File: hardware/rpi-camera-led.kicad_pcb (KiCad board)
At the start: 2 copper layers, 25 x 23.9 mm, 24 parts, among them J1 FFC 15P 1.0mm bottom contact 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, J2 FFC 15P 1.0mm top contact (to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, J3 Qwiic (JST SH 1.0mm), J4 SWD program header 2.54mm, Q1 AO3400A, Q2 Phototransistor, U1 CH32V003A4M6

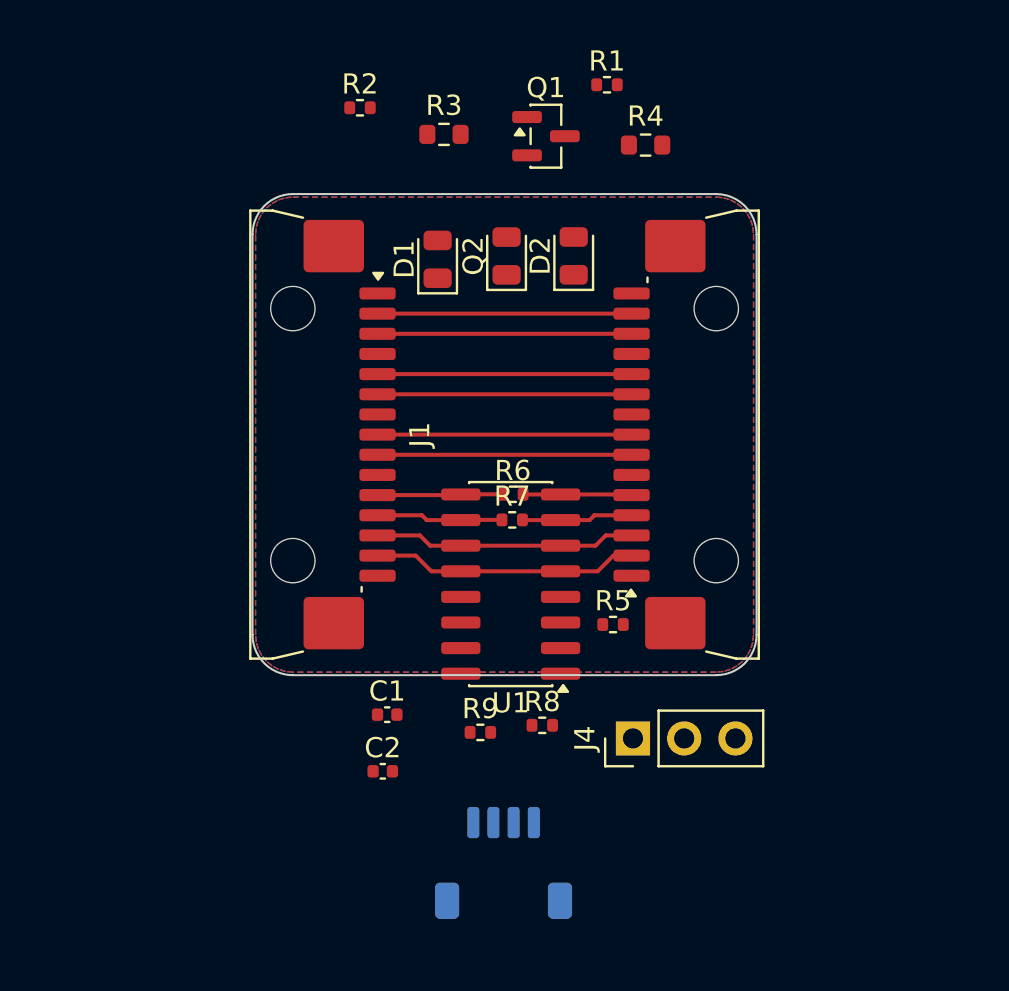
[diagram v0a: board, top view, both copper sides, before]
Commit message: Route camera interposer and prepare manufacturing outputs
Update the CH32V003A4M6 pin mapping, widen and route the board around the camera lens, source the BOM, and add a DRC-gated fabrication export plus approximate assembly CAD renders.

Co-authored-by: Copilot <223556219+Copilot@users.noreply.github.com>
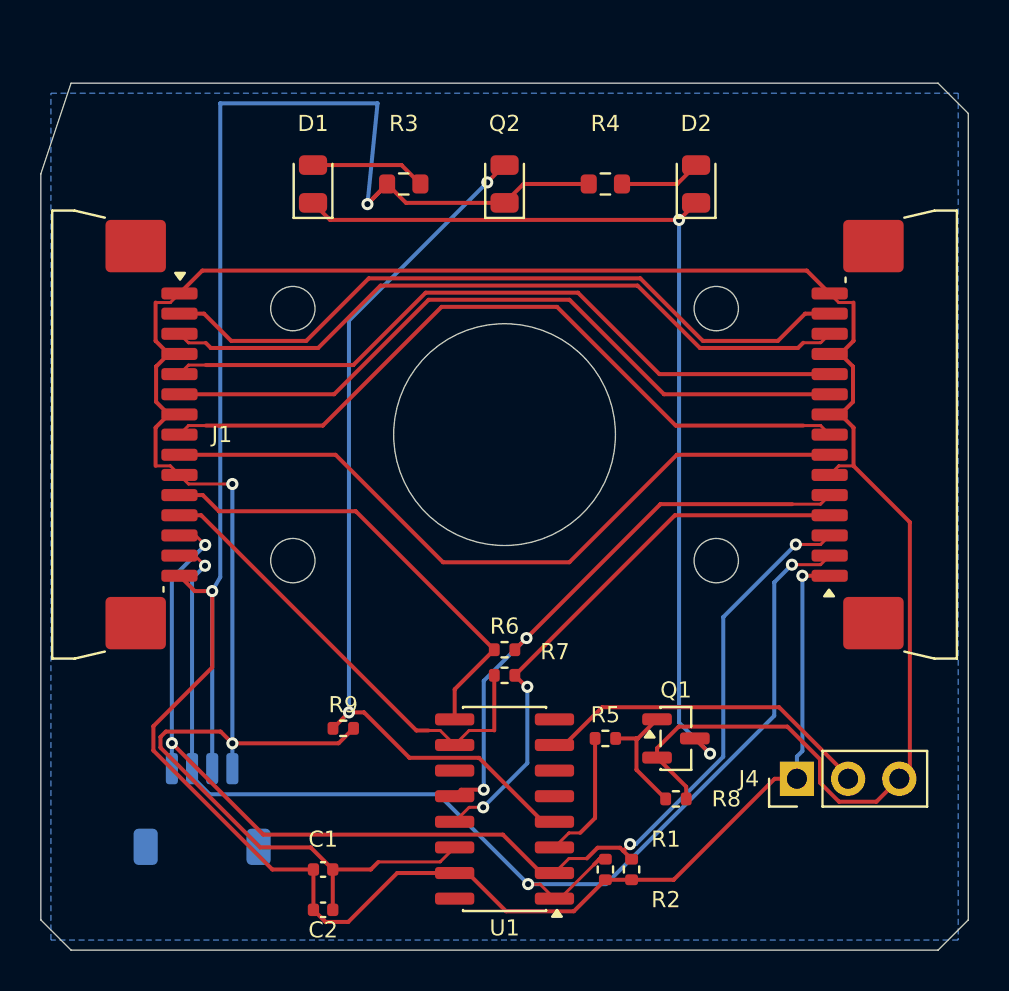
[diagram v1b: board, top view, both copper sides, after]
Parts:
- R3, R4: value 10R -> 47R
- R6, R7: value 0 -> 10k
- moved R2 40.1 mm to (38.8, 53.5), turned to 90 degrees
- moved R1 38.9 mm to (37.5, 53.5), turned to 90 degrees
- moved Q1 30.6 mm to (41.0, 47.0)
- moved J3 15.2 mm to (17.5, 50.5)
- moved U1 11.2 mm to (32.5, 50.5)
- moved J2 9.83 mm to (52.0, 31.9)
- moved J1 9.82 mm to (13.0, 31.9)
- moved J4 8.37 mm to (47.0, 49.0)
- moved C1 8.31 mm to (23.5, 53.5)
- moved R6 7.72 mm to (32.5, 42.6)
- moved R7 7.72 mm to (32.5, 43.9)
- moved R8 7.57 mm to (41.0, 50.0)
- moved C2 7.48 mm to (23.5, 55.5)
- moved D1 7.22 mm to (23.0, 19.5)
- moved D2 7.04 mm to (42.0, 19.5)
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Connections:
- J4 pad 2: CAM_IO1 -> SWIO
- U1 pad 11: SCL -> unconnected-(U1-PD7-Pad11)
- U1 pad 12: SDA -> CAM_IO0
- U1 pad 13: unconnected-(U1-PA2-Pad13) -> CAM_IO1
- U1 pad 5: SDA -> unconnected-(U1-PC6-Pad5)
- U1 pad 6: SCL -> unconnected-(U1-PC7-Pad6)
- U1 pad 7: CAM_IO1 -> SWIO
- U1 pad 8: CAM_IO0 -> unconnected-(U1-PD4-Pad8)
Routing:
- net GND: track 0.00 -> 141.5 mm, vias 0 -> 2
- net 3V3: track 0.00 -> 123.2 mm, vias 0 -> 3
- net SDA: track 13.2 -> 61.6 mm, vias 0 -> 3
- net LED_SW: track 0.00 -> 47.9 mm, vias 0 -> 2
- net SCL: track 13.0 -> 60.3 mm, vias 0 -> 4
- net LIGHT_SENSE: track 0.00 -> 43.9 mm, vias 0 -> 2
- net CAM_CK_N: track 12.6 -> 37.5 mm
- net CAM_CK_P: track 12.6 -> 36.7 mm
- net CAM_D1_P: track 12.6 -> 36.1 mm
- net CAM_IO0: track 5.40 -> 28.8 mm, vias 0 -> 2
- net CAM_D0_N: track 12.6 -> 35.9 mm
- net CAM_D1_N: track 12.6 -> 35.6 mm
- net CAM_IO1: track 5.51 -> 28.4 mm, vias 0 -> 2
- net CAM_D0_P: track 12.6 -> 35.4 mm
- net PI_IO1: track 6.27 -> 23.4 mm
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- removed copper zone on F.Cu, net GND
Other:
- board size 25 x 23.9 mm -> 46 x 43 mm

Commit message: Move Qwiic connector to board edge
Reroute J3, enforce its edge placement in PCB checks, and regenerate the manufacturing and assembly outputs.

Co-authored-by: Copilot <223556219+Copilot@users.noreply.github.com>
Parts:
- moved J3 3.20 mm to (17.5, 53.7)
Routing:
- net 3V3: track 123.2 -> 115.5 mm, vias 3 -> 4
- net SCL: track 60.3 -> 63.5 mm
- net SDA: track 61.6 -> 64.0 mm
- net GND: track 141.5 -> 140.3 mm

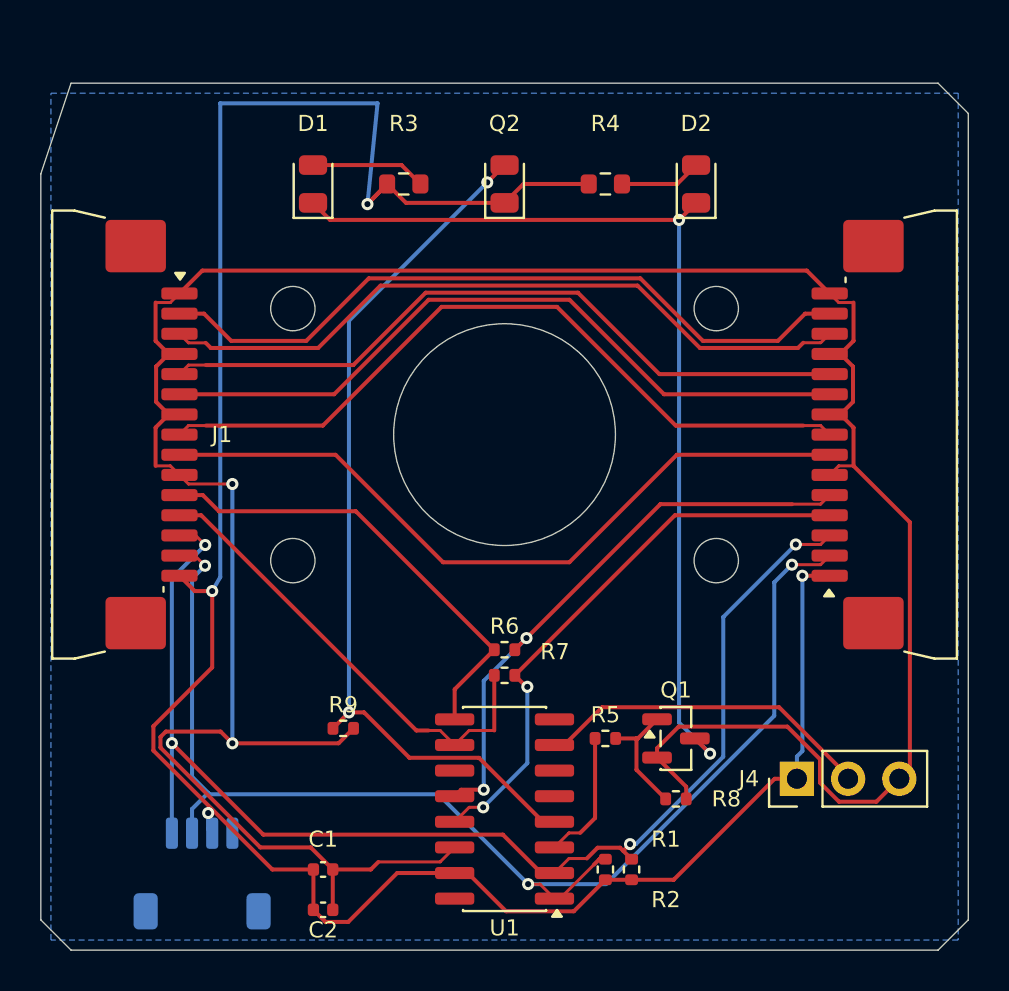
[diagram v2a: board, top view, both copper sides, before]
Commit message: Redesign interposer for supplied camera v3 model
Align the aperture and 20 x 12.5 mm mounting pattern to the supplied camera model, move the LED row, and refresh the routed board, manufacturing export, and assembly fit renders.

Co-authored-by: Copilot <223556219+Copilot@users.noreply.github.com>
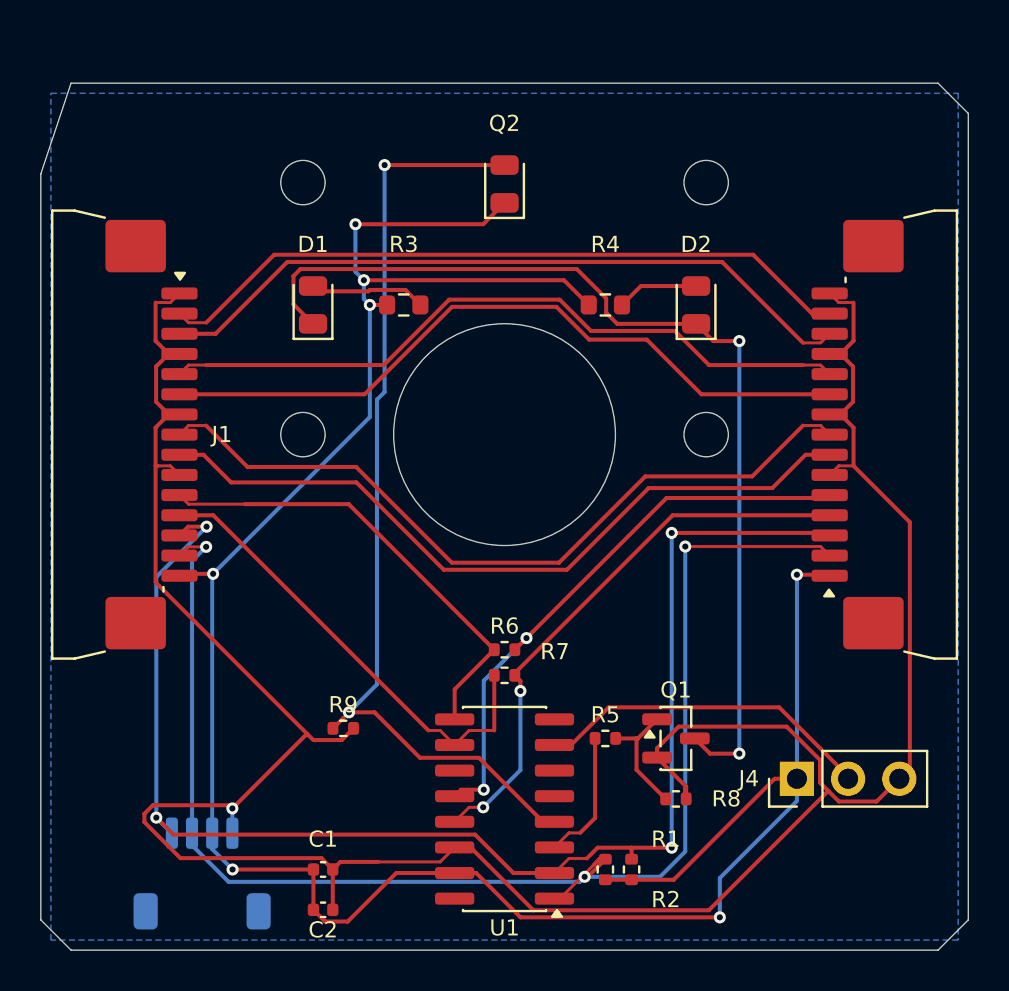
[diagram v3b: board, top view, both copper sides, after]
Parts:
- moved H1 6.27 mm to (22.5, 19.4)
- moved H3 6.27 mm to (42.5, 19.4)
- moved H2 6.27 mm to (22.5, 31.9)
- moved H4 6.27 mm to (42.5, 31.9)
- moved D1 6.00 mm to (23.0, 25.5)
- moved D2 6.00 mm to (42.0, 25.5)
- moved R3 6.00 mm to (27.5, 25.5)
- moved R4 6.00 mm to (37.5, 25.5)
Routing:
- net GND: track 140.3 -> 132.7 mm, vias 2 -> 1
- net SCL: track 63.5 -> 69.4 mm
- net SDA: track 64.0 -> 69.6 mm
- net LIGHT_SENSE: track 43.9 -> 47.4 mm
- net 3V3: track 115.5 -> 118.1 mm, vias 4 -> 7
- net LED_SW: track 47.9 -> 49.9 mm
- net CAM_D0_N: track 35.9 -> 35.0 mm
- net CAM_CK_N: track 37.5 -> 38.3 mm
